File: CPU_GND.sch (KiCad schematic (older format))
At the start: 1 part

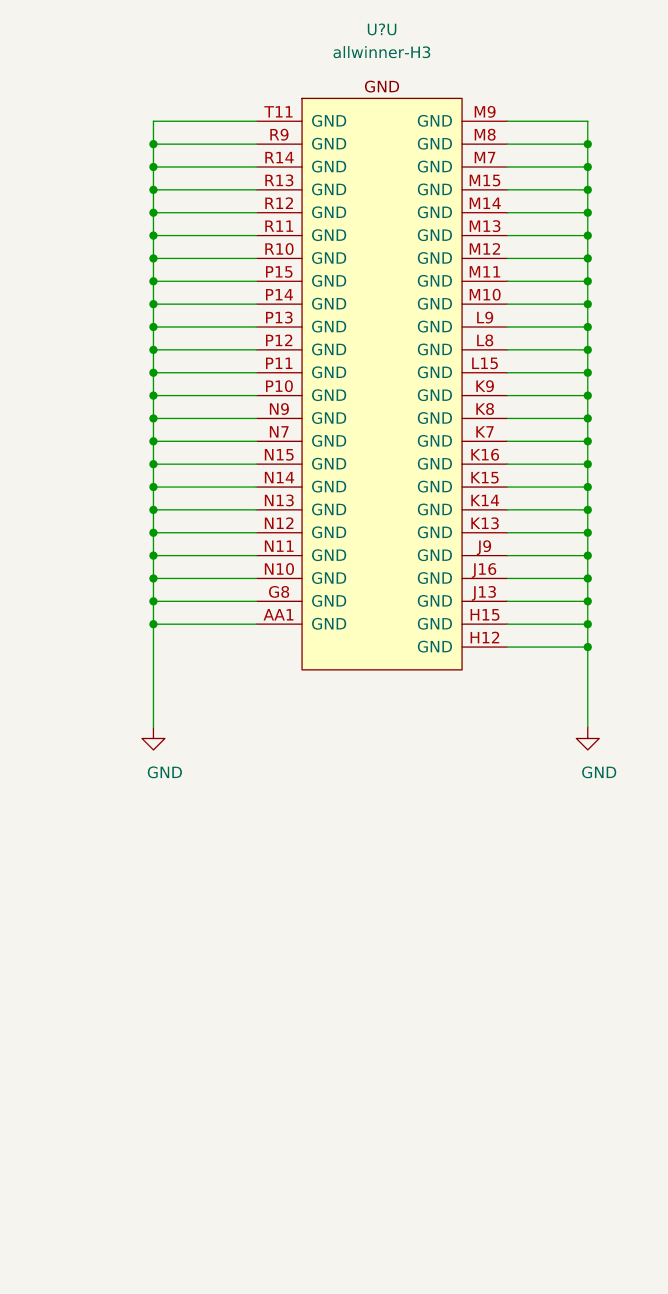
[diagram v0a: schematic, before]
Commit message: update port decouple cap,
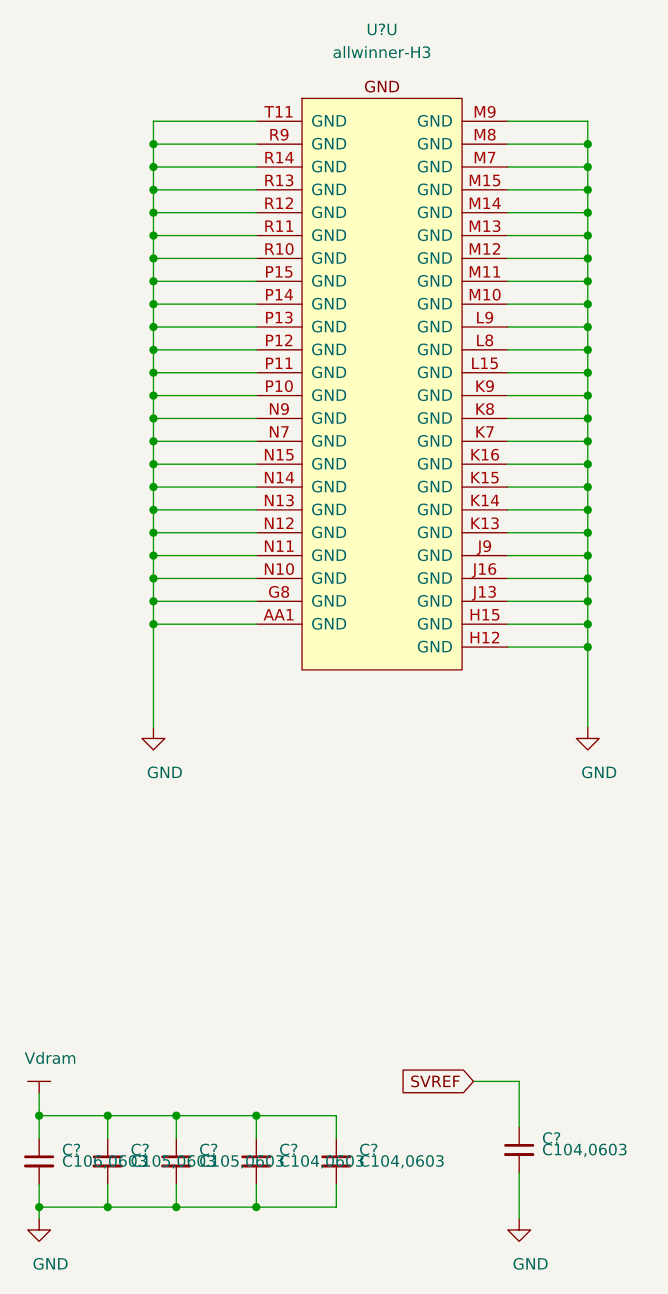
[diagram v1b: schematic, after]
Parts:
- added C?: C106,0603, Capacitor_SMD:C_0603_1608Metric_Pad1.05x0.95mm_HandSolder, symbol taobao-c:C106,0603
- added C? (x2): C105,0603, Capacitor_SMD:C_0603_1608Metric_Pad1.05x0.95mm_HandSolder, symbol taobao-c:C105,0603
- added C? (x3): C104,0603, Capacitor_SMD:C_0603_1608Metric_Pad1.05x0.95mm_HandSolder, symbol taobao-c:C104,0603
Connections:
- net GND: now also C?.2, C?.2, C?.2, C?.2, C?.2, C?.2
- new net SVREF: C?.1
- new net Vdram: C?.1, C?.1, C?.1, C?.1, C?.1

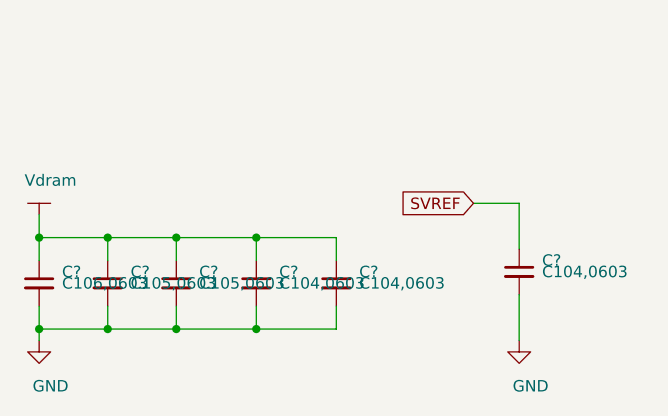
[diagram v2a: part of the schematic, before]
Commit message: update Vdram capacitor,
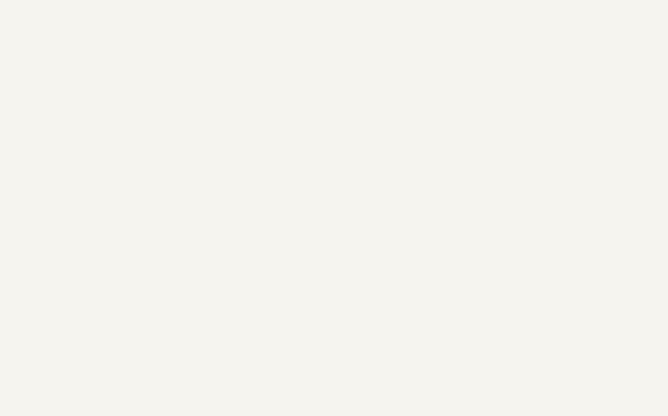
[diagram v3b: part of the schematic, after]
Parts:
- removed C?: C106,0603, Capacitor_SMD:C_0603_1608Metric_Pad1.05x0.95mm_HandSolder, symbol taobao-c:C106,0603
- removed C? (x2): C105,0603, Capacitor_SMD:C_0603_1608Metric_Pad1.05x0.95mm_HandSolder, symbol taobao-c:C105,0603
- removed C? (x3): C104,0603, Capacitor_SMD:C_0603_1608Metric_Pad1.05x0.95mm_HandSolder, symbol taobao-c:C104,0603
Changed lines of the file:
@@
 Connection ~ 6900 6500
 Connection ~ 6900 6600
-$Comp
-L taobao-components:Vdram #PWR?
-U 1 1 5C78ADC4
-P 6400 8650
-AR Path="/5C273FE9/5C786D7F/5C78ADC4" Ref="#PWR?"  Part="1"
-AR Path="/5C273FE9/5C7AC496/5C78ADC4" Ref="#PWR?"  Part="1"
-AR Path="/5C7B767A/5C786D7F/5C78ADC4" Ref="#PWR?"  Part="1"
-F 0 "#PWR?" H 6400 8500 50  0001 C CNN
-F 1 "Vdram" H 6450 8800 50  0000 C CNN
-F 2 "" H 6400 8650 50  0001 C CNN
-F 3 "" H 6400 8650 50  0001 C CNN
-	1    6400 8650
-	1    0    0    -1
-$EndComp
-$Comp
-L taobao-c:C106,0603 C?
-U 1 1 5C78AE8E
-P 6400 8950
-AR Path="/5C273FE9/5C786D7F/5C78AE8E" Ref="C?"  Part="1"
-AR Path="/5C273FE9/5C7AC496/5C78AE8E" Ref="C?"  Part="1"
-AR Path="/5C7B767A/5C786D7F/5C78AE8E" Ref="C?"  Part="1"
-F 0 "C?" H 6500 9000 50  0000 L CNN
-F 1 "C106,0603" H 6500 8950 50  0000 L CNN
-F 2 "Capacitor_SMD:C_0603_1608Metric_Pad1.05x0.95mm_HandSolder" H 6400 8950 50  0001 C CNN
-F 3 "~" H 6400 8950 50  0001 C CNN
-	1    6400 8950
-	1    0    0    -1
-$EndComp
-$Comp
-L power:GND #PWR?
-U 1 1 5C78AF13
-P 6400 9200
-AR Path="/5C273FE9/5C786D7F/5C78AF13" Ref="#PWR?"  Part="1"
-AR Path="/5C273FE9/5C7AC496/5C78AF13" Ref="#PWR?"  Part="1"
-AR Path="/5C7B767A/5C786D7F/5C78AF13" Ref="#PWR?"  Part="1"
-F 0 "#PWR?" H 6400 8950 50  0001 C CNN
-F 1 "GND" H 6450 9000 50  0000 C CNN
-F 2 "" H 6400 9200 50  0001 C CNN
-F 3 "" H 6400 9200 50  0001 C CNN
-	1    6400 9200
-	1    0    0    -1
-$EndComp
-Wire Wire Line
-	6400 9200 6400 9150
 Wire Wire Line
 	8800 4700 8800 4600
@@
 Wire Wire Line
 	6900 6600 6900 7050
-Wire Wire Line
-	6400 8650 6400 8750
-$Comp
-L taobao-c:C105,0603 C?
-U 1 1 5C78EFC9
-P 6700 8950
-AR Path="/5C273FE9/5C786D7F/5C78EFC9" Ref="C?"  Part="1"
-AR Path="/5C273FE9/5C7AC496/5C78EFC9" Ref="C?"  Part="1"
-AR Path="/5C7B767A/5C786D7F/5C78EFC9" Ref="C?"  Part="1"
-F 0 "C?" H 6800 9000 50  0000 L CNN
-F 1 "C105,0603" H 6800 8950 50  0000 L CNN
-F 2 "Capacitor_SMD:C_0603_1608Metric_Pad1.05x0.95mm_HandSolder" H 6700 8950 50  0001 C CNN
-F 3 "~" H 6700 8950 50  0001 C CNN
-	1    6700 8950
-	1    0    0    -1
-$EndComp
-Wire Wire Line
-	6700 8850 6700 8750
-Wire Wire Line
-	6700 8750 6400 8750
-Connection ~ 6400 8750
-Wire Wire Line
-	6400 8750 6400 8850
-Wire Wire Line
-	6700 9050 6700 9150
-Wire Wire Line
-	6700 9150 6400 9150
-Connection ~ 6400 9150
-Wire Wire Line
-	6400 9150 6400 9050
-$Comp
-L taobao-c:C105,0603 C?
-U 1 1 5C793900
-P 7000 8950
-AR Path="/5C273FE9/5C786D7F/5C793900" Ref="C?"  Part="1"
-AR Path="/5C273FE9/5C7AC496/5C793900" Ref="C?"  Part="1"
-AR Path="/5C7B767A/5C786D7F/5C793900" Ref="C?"  Part="1"
-F 0 "C?" H 7100 9000 50  0000 L CNN
-F 1 "C105,0603" H 7100 8950 50  0000 L CNN
-F 2 "Capacitor_SMD:C_0603_1608Metric_Pad1.05x0.95mm_HandSolder" H 7000 8950 50  0001 C CNN
-F 3 "~" H 7000 8950 50  0001 C CNN
-	1    7000 8950
-	1    0    0    -1
-$EndComp
-Wire Wire Line
-	7000 8850 7000 8750
-Wire Wire Line
-	7000 8750 6700 8750
-Wire Wire Line
-	7000 9050 7000 9150
-Wire Wire Line
-	7000 9150 6700 9150
-Connection ~ 6700 8750
-Connection ~ 6700 9150
-$Comp
-L taobao-c:C104,0603 C?
-U 1 1 5C79656A
-P 7350 8950
-AR Path="/5C273FE9/5C786D7F/5C79656A" Ref="C?"  Part="1"
-AR Path="/5C273FE9/5C7AC496/5C79656A" Ref="C?"  Part="1"
-AR Path="/5C7B767A/5C786D7F/5C79656A" Ref="C?"  Part="1"
-F 0 "C?" H 7450 9000 50  0000 L CNN
-F 1 "C104,0603" H 7450 8950 50  0000 L CNN
-F 2 "Capacitor_SMD:C_0603_1608Metric_Pad1.05x0.95mm_HandSolder" H 7350 8950 50  0001 C CNN
-F 3 "~" H 7350 8950 50  0001 C CNN
-	1    7350 8950
-	1    0    0    -1
-$EndComp
-Wire Wire Line
-	7350 8850 7350 8750
-Wire Wire Line
-	7350 8750 7000 8750
-Connection ~ 7000 8750
-Wire Wire Line
-	7350 9050 7350 9150
-Wire Wire Line
-	7350 9150 7000 9150
-Connection ~ 7000 9150
-$Comp
-L taobao-c:C104,0603 C?
-U 1 1 5C79C1D5
-P 7700 8950
-AR Path="/5C273FE9/5C786D7F/5C79C1D5" Ref="C?"  Part="1"
-AR Path="/5C273FE9/5C7AC496/5C79C1D5" Ref="C?"  Part="1"
-AR Path="/5C7B767A/5C786D7F/5C79C1D5" Ref="C?"  Part="1"
-F 0 "C?" H 7800 9000 50  0000 L CNN
-F 1 "C104,0603" H 7800 8950 50  0000 L CNN
-F 2 "Capacitor_SMD:C_0603_1608Metric_Pad1.05x0.95mm_HandSolder" H 7700 8950 50  0001 C CNN
-F 3 "~" H 7700 8950 50  0001 C CNN
-	1    7700 8950
-	1    0    0    -1
-$EndComp
-Wire Wire Line
-	7700 8850 7700 8750
-Wire Wire Line
-	7700 8750 7350 8750
-Wire Wire Line
-	7700 9050 7700 9150
-Wire Wire Line
-	7700 9150 7350 9150
-Connection ~ 7350 8750
-Connection ~ 7350 9150
-Text GLabel 8300 8600 0    50   Input ~ 0
-SVREF
-$Comp
-L taobao-c:C104,0603 C?
-U 1 1 5C79F6B1
-P 8500 8900
-AR Path="/5C273FE9/5C786D7F/5C79F6B1" Ref="C?"  Part="1"
-AR Path="/5C273FE9/5C7AC496/5C79F6B1" Ref="C?"  Part="1"
-AR Path="/5C7B767A/5C786D7F/5C79F6B1" Ref="C?"  Part="1"
-F 0 "C?" H 8600 8950 50  0000 L CNN
-F 1 "C104,0603" H 8600 8900 50  0000 L CNN
-F 2 "Capacitor_SMD:C_0603_1608Metric_Pad1.05x0.95mm_HandSolder" H 8500 8900 50  0001 C CNN
-F 3 "~" H 8500 8900 50  0001 C CNN
-	1    8500 8900
-	1    0    0    -1
-$EndComp
-Wire Wire Line
-	8300 8600 8500 8600
-Wire Wire Line
-	8500 8600 8500 8800
-$Comp
-L power:GND #PWR?
-U 1 1 5C7A613A
-P 8500 9200
-AR Path="/5C273FE9/5C786D7F/5C7A613A" Ref="#PWR?"  Part="1"
-AR Path="/5C273FE9/5C7AC496/5C7A613A" Ref="#PWR?"  Part="1"
-AR Path="/5C7B767A/5C786D7F/5C7A613A" Ref="#PWR?"  Part="1"
-F 0 "#PWR?" H 8500 8950 50  0001 C CNN
-F 1 "GND" H 8550 9000 50  0000 C CNN
-F 2 "" H 8500 9200 50  0001 C CNN
-F 3 "" H 8500 9200 50  0001 C CNN
-	1    8500 9200
-	1    0    0    -1
-$EndComp
-Wire Wire Line
-	8500 9200 8500 9000
 $EndSCHEMATC
